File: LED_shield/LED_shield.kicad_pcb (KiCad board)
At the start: 4 copper layers, 79 x 80 mm, 119 parts, among them J103 Screw_Terminal_01x02, J104 Screw_Terminal_01x02, J105 Screw_Terminal_01x02, J106 Screw_Terminal_01x02, J107 Screw_Terminal_01x02, J108 Screw_Terminal_01x02, J109 Screw_Terminal_01x03, J110 Screw_Terminal_01x03, J111 Screw_Terminal_01x03, J112 Screw_Terminal_01x03, J113 Screw_Terminal_01x03, J114 Screw_Terminal_01x03, J301 Screw_Terminal_01x02, Q201 PMOS, Q301 NMOS, Q302 NMOS, Q303 NMOS, Q304 NMOS, Q305 NMOS, SW201 SW_DIP_x08, SW202 SW_DIP_x08, U201 74HC165, U202 7414, U203 7414, U204 74HC165, U301 LM74700, U302 LM25149RGYR, U303 LM25149RGYR

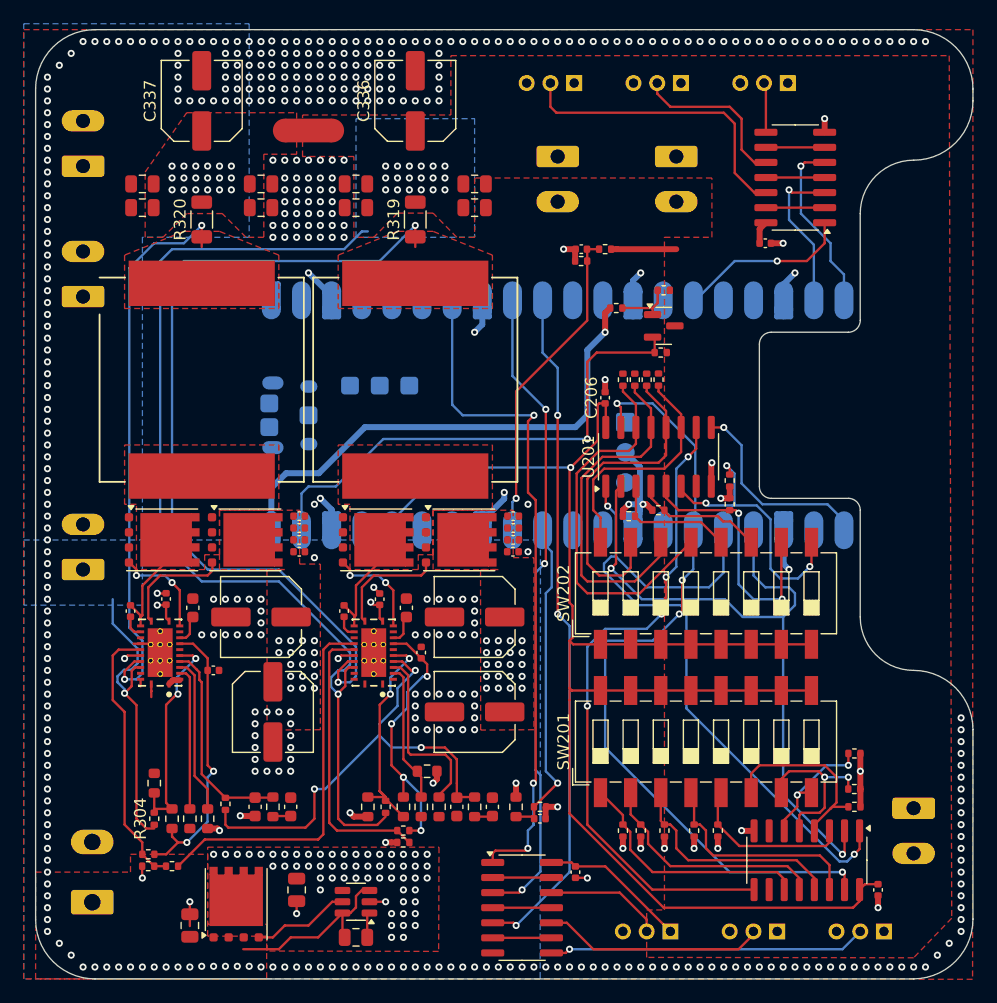
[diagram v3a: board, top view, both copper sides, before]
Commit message: Make PCB ready for manufacture (again)
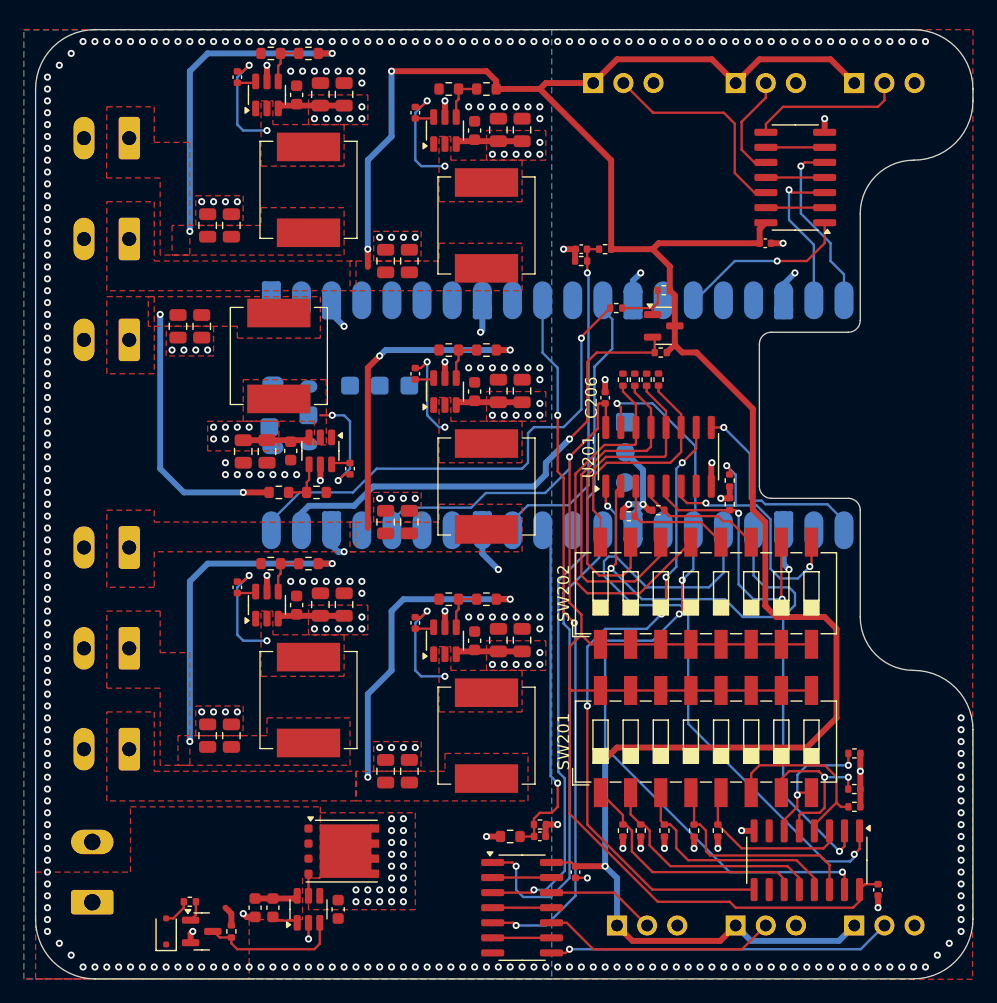
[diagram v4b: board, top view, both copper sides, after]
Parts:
- removed C304, C307, C326, C327: 100n, Capacitor_SMD:C_0402_1005Metric
- removed C305, C306, C308, C309: 22u, Capacitor_SMD:C_Elec_6.3x5.8
- removed C310, C311, C314, C315, C318, C319, C320, C321, C322, C323: 10n, Capacitor_SMD:C_0402_1005Metric
- removed C312, C313: 5.6nF, Capacitor_SMD:C_0603_1608Metric
- removed C316, C317: 470pF, Capacitor_SMD:C_0603_1608Metric
- removed C324, C325: 2.2uF, Capacitor_SMD:C_0603_1608Metric
- removed C328, C329, C330, C331, C332, C333, C334, C335: 22uF, Capacitor_SMD:C_0805_2012Metric
- removed C336, C337: 180uF, Capacitor_SMD:C_Elec_6.3x5.8
- removed J103, J104, J105, J106, J107, J108: Screw_Terminal_01x02, Connector_Phoenix_MC:PhoenixContact_MCV_1,5_2-G-3.81_1x02_P3.81mm_Vertical
- removed L301, L302: 4.7u, Inductor_SMD:L_Vishay_IHLP-6767
- removed NT301: NetTie_2, NetTie:NetTie-2_SMD_Pad2.0mm
- removed Q302, Q303, Q304, Q305: NMOS, Package_SON:VSONP-8-1EP_5x6_P1.27mm
- removed R301, R312, R315, R316, R317, R318: 0R, Resistor_SMD:R_0402_1005Metric
- removed R302, R304: 100k, Resistor_SMD:R_0402_1005Metric
- removed R303, R305: 19k1, Resistor_SMD:R_0603_1608Metric
- removed R306, R307: 5k1, Resistor_SMD:R_0603_1608Metric
- removed R308, R309: 24k, Resistor_SMD:R_0603_1608Metric
- removed R310: 560k, Resistor_SMD:R_0603_1608Metric
- removed R311: 91k, Resistor_SMD:R_0603_1608Metric
- removed R313, R314: 75k, Resistor_SMD:R_0603_1608Metric
- removed R319, R320: 5m, Resistor_SMD:R_1206_3216Metric
- removed R321: 82k, Resistor_SMD:R_0603_1608Metric
- removed U302, U303: LM25149RGYR, Skrooter_footprints:RGY0024E-MFG
- added C401: 10u, Capacitor_SMD:C_0805_2012Metric, F.Cu at (75.0, 38.0)
- added C402: 10u, Capacitor_SMD:C_0805_2012Metric, F.Cu at (77.0, 38.0)
- added C403: 100n, Capacitor_SMD:C_0603_1608Metric, F.Cu at (73.0, 38.0)
- added C404: 100n, Capacitor_SMD:C_0402_1005Metric, F.Cu at (68.0, 36.5)
- added C405: 22u, Capacitor_SMD:C_0805_2012Metric, F.Cu at (65.5, 49.0)
- added C406: 22u, Capacitor_SMD:C_0805_2012Metric, F.Cu at (67.5, 49.0)
- added C501: 10u, Capacitor_SMD:C_0805_2012Metric, F.Cu at (90.0, 41.0)
- added C502: 10u, Capacitor_SMD:C_0805_2012Metric, F.Cu at (92.0, 41.0)
- added C503: 100n, Capacitor_SMD:C_0603_1608Metric, F.Cu at (88.0, 41.0)
- added C504: 100n, Capacitor_SMD:C_0402_1005Metric, F.Cu at (83.0, 39.5)
- added C505: 22u, Capacitor_SMD:C_0805_2012Metric, F.Cu at (80.5, 52.0)
- added C506: 22u, Capacitor_SMD:C_0805_2012Metric, F.Cu at (82.5, 52.0)
- added C601: 10u, Capacitor_SMD:C_0805_2012Metric, F.Cu at (70.5, 68.0)
- added C602: 10u, Capacitor_SMD:C_0805_2012Metric, F.Cu at (68.5, 68.0)
- added C603: 100n, Capacitor_SMD:C_0603_1608Metric, F.Cu at (72.5, 68.0)
- added C604: 100n, Capacitor_SMD:C_0402_1005Metric, F.Cu at (77.5, 69.5)
- added C605: 22u, Capacitor_SMD:C_0805_2012Metric, F.Cu at (65.0, 57.5)
- added C606: 22u, Capacitor_SMD:C_0805_2012Metric, F.Cu at (63.0, 57.5)
- added C701: 10u, Capacitor_SMD:C_0805_2012Metric, F.Cu at (90.0, 63.0)
- added C702: 10u, Capacitor_SMD:C_0805_2012Metric, F.Cu at (92.0, 63.0)
- added C703: 100n, Capacitor_SMD:C_0603_1608Metric, F.Cu at (88.0, 63.0)
- added C704: 100n, Capacitor_SMD:C_0402_1005Metric, F.Cu at (83.0, 61.5)
- added C705: 22u, Capacitor_SMD:C_0805_2012Metric, F.Cu at (80.5, 74.0)
- added C706: 22u, Capacitor_SMD:C_0805_2012Metric, F.Cu at (82.5, 74.0)
- added C801: 10u, Capacitor_SMD:C_0805_2012Metric, F.Cu at (75.0, 81.0)
- added C802: 10u, Capacitor_SMD:C_0805_2012Metric, F.Cu at (77.0, 81.0)
- added C803: 100n, Capacitor_SMD:C_0603_1608Metric, F.Cu at (73.0, 81.0)
- added C804: 100n, Capacitor_SMD:C_0402_1005Metric, F.Cu at (68.0, 79.5)
- added C805: 22u, Capacitor_SMD:C_0805_2012Metric, F.Cu at (65.5, 92.0)
- added C806: 22u, Capacitor_SMD:C_0805_2012Metric, F.Cu at (67.5, 92.0)
- added C901: 10u, Capacitor_SMD:C_0805_2012Metric, F.Cu at (90.0, 84.0)
- added C902: 10u, Capacitor_SMD:C_0805_2012Metric, F.Cu at (92.0, 84.0)
- added C903: 100n, Capacitor_SMD:C_0603_1608Metric, F.Cu at (88.0, 84.0)
- added C904: 100n, Capacitor_SMD:C_0402_1005Metric, F.Cu at (83.0, 82.5)
- added C905: 22u, Capacitor_SMD:C_0805_2012Metric, F.Cu at (80.5, 95.0)
- added C906: 22u, Capacitor_SMD:C_0805_2012Metric, F.Cu at (82.5, 95.0)
- added D1: BZT52-C16S-AU, Diode_SMD:D_SOD-323F, F.Cu at (62.0, 108.5)
- added J1: Screw_Terminal_01x02, Connector_Phoenix_MC:PhoenixContact_MCV_1,5_2-G-3.81_1x02_P3.81mm_Vertical, B.Cu at (58.9, 41.6)
- added J2: Screw_Terminal_01x02, Connector_Phoenix_MC:PhoenixContact_MCV_1,5_2-G-3.81_1x02_P3.81mm_Vertical, B.Cu at (58.9, 50.1)
- added J3: Screw_Terminal_01x02, Connector_Phoenix_MC:PhoenixContact_MCV_1,5_2-G-3.81_1x02_P3.81mm_Vertical, B.Cu at (58.9, 58.6)
- added J4: Screw_Terminal_01x02, Connector_Phoenix_MC:PhoenixContact_MCV_1,5_2-G-3.81_1x02_P3.81mm_Vertical, B.Cu at (58.9, 76.1)
- added J5: Screw_Terminal_01x02, Connector_Phoenix_MC:PhoenixContact_MCV_1,5_2-G-3.81_1x02_P3.81mm_Vertical, B.Cu at (58.9, 84.6)
- added J6: Screw_Terminal_01x02, Connector_Phoenix_MC:PhoenixContact_MCV_1,5_2-G-3.81_1x02_P3.81mm_Vertical, B.Cu at (58.9, 93.1)
- added L401: 3.3u, Skrooter_footprints:IHLP3232, F.Cu at (74.0, 46.0)
- added L501: 3.3u, Skrooter_footprints:IHLP3232, F.Cu at (89.0, 49.0)
- added L601: 3.3u, Skrooter_footprints:IHLP3232, F.Cu at (71.5, 60.0)
- added L701: 3.3u, Skrooter_footprints:IHLP3232, F.Cu at (89.0, 71.0)
- added L801: 3.3u, Skrooter_footprints:IHLP3232, F.Cu at (74.0, 89.0)
- added L901: 3.3u, Skrooter_footprints:IHLP3232, F.Cu at (89.0, 92.0)
- added Q1: MMBT5551L, Package_TO_SOT_SMD:SOT-23, F.Cu at (65.0, 108.5)
- added R1: 100k, Resistor_SMD:R_0402_1005Metric, F.Cu at (67.5, 108.5)
- added R2: 100k, Resistor_SMD:R_0402_1005Metric, F.Cu at (64.0, 106.0)
- added R401: 56k, Resistor_SMD:R_0603_1608Metric, F.Cu at (74.0, 34.5)
- added R402: 10k, Resistor_SMD:R_0603_1608Metric, F.Cu at (70.8, 34.5)
- added R501: 56k, Resistor_SMD:R_0603_1608Metric, F.Cu at (89.0, 37.5)
- added R502: 10k, Resistor_SMD:R_0603_1608Metric, F.Cu at (85.8, 37.5)
- added R601: 56k, Resistor_SMD:R_0603_1608Metric, F.Cu at (71.5, 71.5)
- added R602: 10k, Resistor_SMD:R_0603_1608Metric, F.Cu at (74.7, 71.5)
- added R701: 56k, Resistor_SMD:R_0603_1608Metric, F.Cu at (89.0, 59.5)
- added R702: 10k, Resistor_SMD:R_0603_1608Metric, F.Cu at (85.8, 59.5)
- added R801: 56k, Resistor_SMD:R_0603_1608Metric, F.Cu at (74.0, 77.5)
- added R802: 10k, Resistor_SMD:R_0603_1608Metric, F.Cu at (70.8, 77.5)
- added R901: 56k, Resistor_SMD:R_0603_1608Metric, F.Cu at (89.0, 80.5)
- added R902: 10k, Resistor_SMD:R_0603_1608Metric, F.Cu at (85.8, 80.5)
- added U401: TPS565208, Package_TO_SOT_SMD:SOT-23-6, F.Cu at (70.5, 38.0)
- added U501: TPS565208, Package_TO_SOT_SMD:SOT-23-6, F.Cu at (85.5, 41.0)
- added U601: TPS565208, Package_TO_SOT_SMD:SOT-23-6, F.Cu at (75.0, 68.0)
- added U701: TPS565208, Package_TO_SOT_SMD:SOT-23-6, F.Cu at (85.5, 63.0)
- added U801: TPS565208, Package_TO_SOT_SMD:SOT-23-6, F.Cu at (70.5, 81.0)
- added U901: TPS565208, Package_TO_SOT_SMD:SOT-23-6, F.Cu at (85.5, 84.0)
- C301, C302, C303: footprint Capacitor_SMD:C_0805_2012Metric -> Capacitor_SMD:C_0603_1608Metric
- J109, J110, J111, J112, J113, J114: footprint Connector_PinHeader_2.00mm:PinHeader_1x03_P2.00mm_Vertical -> Connector_PinHeader_2.54mm:PinHeader_1x03_P2.54mm_Vertical
- moved Q301 9.95 mm to (76.8, 101.7), turned to 0 degrees
- moved C301 7.43 mm to (71.0, 106.5), turned to -90 degrees
- moved C302 5.70 mm to (69.5, 106.5), turned to 90 degrees
- moved J109 5.61 mm to (120.0, 37.0), turned to -90 degrees
- moved J110 4.61 mm to (110.0, 37.0), turned to -90 degrees
- moved J114 4.53 mm to (100.0, 108.0), turned to -90 degrees
- moved U301 4.05 mm to (74.0, 106.6), turned to 90 degrees
- moved C303 3.86 mm to (76.5, 106.6)
- moved J113 3.54 mm to (110.0, 108.0), turned to -90 degrees
- moved J112 2.55 mm to (120.0, 108.0), turned to -90 degrees
- moved R204 2.55 mm to (91.0, 100.5), turned to 0 degrees
- moved J111 1.61 mm to (98.0, 37.0), turned to -90 degrees
- moved C201 1.49 mm to (93.5, 100.5)
- moved R205 1.49 mm to (93.5, 99.5)
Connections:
- net /IO/VIN renamed /power/VIN
- A202 pad 12: /IO/DMX_{2}IN_MCU -> /IO/LED4_MCU
- A202 pad 17: /IO/DMX_{1}IN_MCU -> unconnected-(A202-GPIO13-Pad17)
- A202 pad 29: unconnected-(A202-GPIO22-Pad29) -> /IO/LED5_MCU
- A202 pad 7: /IO/LED5_MCU -> unconnected-(A202-GPIO5-Pad7)
- A202 pad 9: /IO/LED4_MCU -> unconnected-(A202-GPIO6-Pad9)
- U301 pad 3: /power/VIN_CONN -> /power/PROT_EN
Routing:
- net +5V: track 104.6 -> 203.7 mm, vias 19 -> 4
- net /power/ISNS+_{1}: track 72.2 -> 0.00 mm, vias 2 -> 0
- net /power/ISNS+_{2}: track 48.1 -> 0.00 mm, vias 2 -> 0
- net /power/EXTCOMP: track 40.0 -> 0.00 mm, vias 3 -> 0
- net /power/VIN: track 8.40 -> 43.2 mm, vias 98 -> 65
- net /power/PG/SYNCOUT_{1}: track 31.7 -> 0.00 mm
- net /power/DCDC3/5V_{OUT}: track 0.00 -> 27.3 mm, vias 0 -> 2
- net /power/DCDC4/5V_{OUT}: track 0.00 -> 27.3 mm, vias 0 -> 2
- net /power/DCDC0/5V_{OUT}: track 0.00 -> 27.3 mm, vias 0 -> 2
- net /power/DCDC5/5V_{OUT}: track 0.00 -> 26.4 mm, vias 0 -> 2
- net /power/+5V_{b}: track 25.9 -> 0.00 mm, vias 19 -> 0
- net /power/VDDA_{2}: track 24.1 -> 0.00 mm, vias 2 -> 0
- net Net-(U302-PFM/SYNC): track 24.0 -> 0.00 mm
- net /power/DCDC2/5V_{OUT}: track 0.00 -> 23.0 mm, vias 0 -> 2
- net Net-(U303-PFM/SYNC): track 22.8 -> 0.00 mm
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- added copper zone on F.Cu, net /power/DCDC0/5V_{OUT}
- added copper zone on F.Cu, net /power/DCDC0/SW
- added copper zone on F.Cu, net /power/DCDC1/SW
- added copper zone on F.Cu, net /power/DCDC2/5V_{OUT}
- added copper zone on F.Cu, net /power/DCDC2/SW
- added copper zone on F.Cu, net /power/DCDC3/5V_{OUT}
- added copper zone on F.Cu, net /power/DCDC3/SW
- added copper zone on F.Cu, net /power/DCDC4/5V_{OUT}
- added copper zone on F.Cu, net /power/DCDC4/SW
- added copper zone on F.Cu, net /power/DCDC5/5V_{OUT}
- added copper zone on F.Cu, net /power/DCDC5/SW
- removed copper zone on B.Cu, net +5V
- removed copper zone on B.Cu, net /power/+5V_{b}
- removed copper zone on F.Cu, net /power/+5V_{b}
- removed copper zone on F.Cu, net /power/DCDC_{1}SW
- removed copper zone on F.Cu, net /power/DCDC_{2}SW
- removed copper zone on F.Cu, net /power/ISNS+_{1}
- removed copper zone on F.Cu, net /power/ISNS+_{2}

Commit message: Add missing LCSC partnumbers
Also fixed grouping in PCB
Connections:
- A202 pad 11: /IO/DMX_{2}OUT_MCU -> unconnected-(A202-GPIO8-Pad11)
- A202 pad 14: /IO/btn_read0 -> unconnected-(A202-GPIO10-Pad14)
- A202 pad 16: /IO/DMX_{1}OUT_MCU -> unconnected-(A202-GPIO12-Pad16)
